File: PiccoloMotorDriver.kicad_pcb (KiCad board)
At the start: 6 copper layers, 55 x 50 mm, 128 parts, among them J1 01x03_MotorTerminal, J10 AUX2, J11 C189893, J12 C265111, J3 C189893, J4 C225127, J5 Screw_Terminal_01x02_POWER, J6 Connector, USB-TYPE-C-16P, J7 C225127, J8 AUX0, J9 AUX1, U1 SP485EEN, U2 XC6210B332MR, U3 XL1509, U4 TJA1050T/CM,118, U5 AS5047D, U6 USBLC6-2SC6, U7 STM32H723VGHx, U8 DRV8316RRGFR, X2 X322516MLB4SI

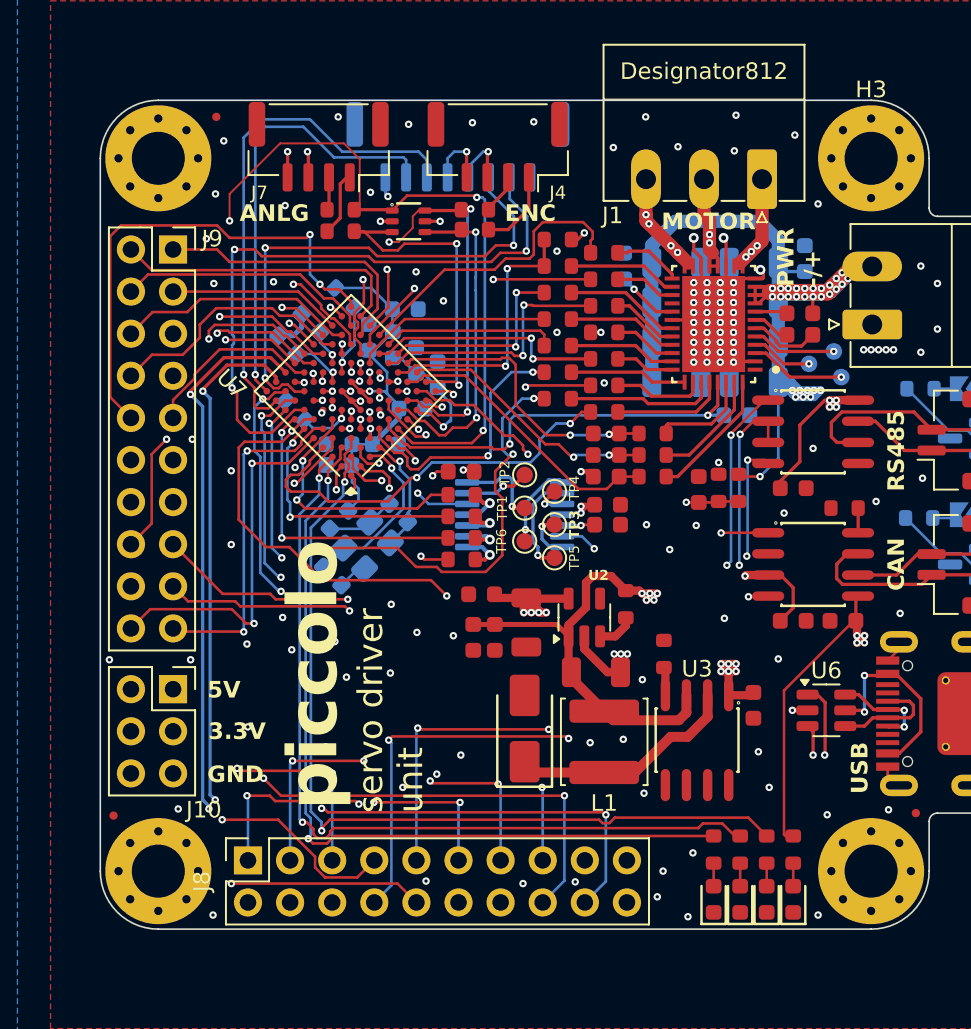
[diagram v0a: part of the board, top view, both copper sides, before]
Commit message: Started discrete inverter version
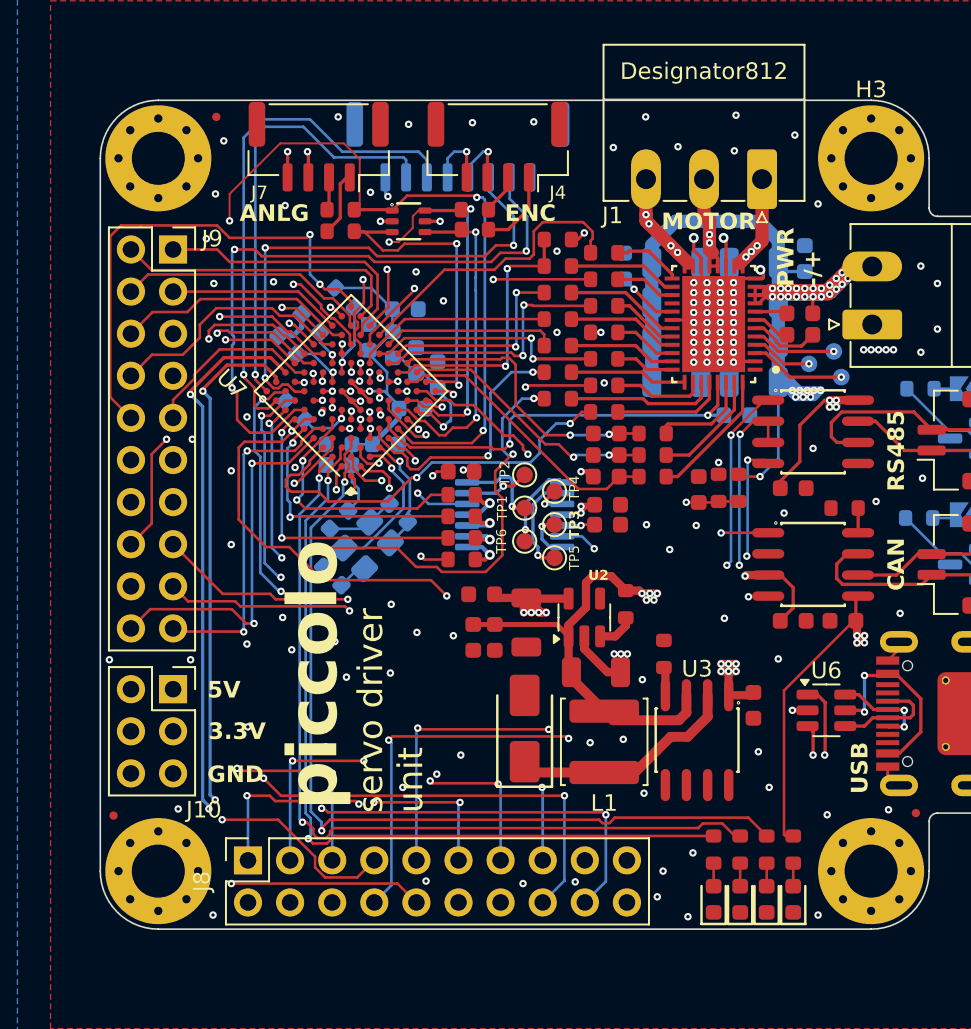
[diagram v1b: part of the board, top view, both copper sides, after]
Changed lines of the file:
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@@
 			(size 0.6 0.6)
 			(drill 0.6)
-			(layers "F&B.Cu" "*.Mask")
+			(layers "*.Cu" "*.Mask")
 		)
 		(pad "" np_thru_hole circle
@@
 			(size 0.6 0.6)
 			(drill 0.6)
-			(layers "F&B.Cu" "*.Mask")
+			(layers "*.Cu" "*.Mask")
 		)
 		(pad "A5" smd rect
@@
 		(tags "connector JST GH horizontal")
 		(property "Reference" "J12"
-			(at 0 3.9 0)
+			(at -3.425 3.9 0)
 			(layer "B.SilkS")
 			(effects
@@
 	)
 	(gr_line
-		(start 167.5 82)
-		(end 163.5 82)
+		(start 113.000026 78.500026)
+		(end 113 121.5)
 		(stroke
 			(width 0.1)
-			(type solid)
+			(type default)
 		)
 		(layer "Edge.Cuts")
 	)
 	(gr_arc
-		(start 163.5 82)
-		(mid 163.146447 81.853553)
-		(end 163 81.5)
+		(start 113.000026 78.500026)
+		(mid 114.025152 76.025152)
+		(end 116.500026 75.000026)
 		(stroke
 			(width 0.1)
@@
 		(layer "Edge.Cuts")
 	)
-	(gr_arc
-		(start 167.5 82)
-		(mid 167.853553 82.146447)
-		(end 168 82.5)
+	(gr_line
+		(start 116.5 125.000026)
+		(end 159.499974 125)
 		(stroke
 			(width 0.1)
@@
 	(gr_line
 		(start 159.500026 75.000026)
-		(end 116.500026 75.000026)
+		(end 116.5 75)
 		(stroke
 			(width 0.1)
@@
 		(layer "Edge.Cuts")
 	)
-	(gr_line
-		(start 163.000004 81.5)
-		(end 163.000026 78.507513)
+	(gr_arc
+		(start 159.500026 75.000026)
+		(mid 161.9749 76.025152)
+		(end 163.000026 78.500026)
 		(stroke
 			(width 0.1)
@@
 	)
 	(gr_line
+		(start 163.000004 81.5)
+		(end 163.000026 78.507513)
+		(stroke
+			(width 0.1)
+			(type default)
+		)
+		(layer "Edge.Cuts")
+	)
+	(gr_arc
+		(start 163.000026 121.500026)
+		(mid 161.9749 123.9749)
+		(end 159.500026 125.000026)
+		(stroke
+			(width 0.1)
+			(type default)
+		)
+		(layer "Edge.Cuts")
+	)
+	(gr_line
 		(start 163.000026 121.500026)
 		(end 163.000026 118.5)
@@
 	)
 	(gr_arc
-		(start 159.500026 75.000026)
-		(mid 161.9749 76.025152)
-		(end 163.000026 78.500026)
+		(start 163.5 82)
+		(mid 163.146447 81.853553)
+		(end 163 81.5)
 		(stroke
 			(width 0.1)
@@
 	)
 	(gr_line
-		(start 168 117.5)
-		(end 168 82.5)
+		(start 163.5 118)
+		(end 167.5 118)
 		(stroke
 			(width 0.1)
@@
 	)
 	(gr_line
-		(start 113.000026 78.500026)
-		(end 113.000026 121.500026)
+		(start 167.5 82)
+		(end 163.5 82)
 		(stroke
 			(width 0.1)
-			(type default)
+			(type solid)
 		)
 		(layer "Edge.Cuts")
 	)
 	(gr_arc
-		(start 113.000026 78.500026)
-		(mid 114.025152 76.025152)
-		(end 116.500026 75.000026)
+		(start 167.5 82)
+		(mid 167.853553 82.146447)
+		(end 168 82.5)
 		(stroke
 			(width 0.1)
@@
 	)
 	(gr_line
-		(start 116.500026 125.000026)
-		(end 159.500026 125.000026)
-		(stroke
-			(width 0.1)
-			(type default)
-		)
-		(layer "Edge.Cuts")
-	)
-	(gr_line
-		(start 163.5 118)
-		(end 167.5 118)
+		(start 168 117.5)
+		(end 168 82.5)
 		(stroke
 			(width 0.1)
@@
 		(layer "Edge.Cuts")
 	)
-	(gr_arc
-		(start 163.000026 121.500026)
-		(mid 161.9749 123.9749)
-		(end 159.500026 125.000026)
-		(stroke
-			(width 0.1)
-			(type default)
+	(gr_text "5V"
+		(at 119.45 111.15 0)
+		(layer "F.SilkS" knockout)
+		(effects
+			(font
+				(size 1 1)
+				(thickness 0.25)
+				(bold yes)
+			)
+			(justify left bottom)
 		)
-		(layer "Edge.Cuts")
 	)
 	(gr_text "GND"
@@
 		)
 	)
-	(gr_text "MOTOR"
-		(at 146.85 82.9 0)
+	(gr_text "3.3V"
+		(at 119.5 113.65 0)
 		(layer "F.SilkS" knockout)
 		(effects
@@
 		)
 	)
+	(gr_text "ENC"
+		(at 137.4 82.4 0)
+		(layer "F.SilkS" knockout)
+		(effects
+			(font
+				(size 1 1)
+				(thickness 0.25)
+				(bold yes)
+			)
+			(justify left bottom)
+		)
+	)
+	(gr_text "MOTOR"
+		(at 146.85 82.9 0)
+		(layer "F.SilkS" knockout)
+		(effects
+			(font
+				(size 1 1)
+				(thickness 0.25)
+				(bold yes)
+			)
+			(justify left bottom)
+		)
+	)
+	(gr_text "PWR\n-/+"
+		(at 156.55 86.25 90)
+		(layer "F.SilkS" knockout)
+		(effects
+			(font
+				(size 1 1)
+				(thickness 0.25)
+				(bold yes)
+			)
+			(justify left bottom)
+		)
+	)
 	(gr_text "USB"
 		(at 159.4 116.85 90)
@@
 		)
 	)
+	(gr_text "RS485"
+		(at 161.6 98.6 90)
+		(layer "F.SilkS" knockout)
+		(effects
+			(font
+				(size 1 1)
+				(thickness 0.25)
+				(bold yes)
+			)
+			(justify left bottom)
+		)
+	)
+	(gr_text "CAN"
+		(at 161.6 104.6 90)
+		(layer "F.SilkS" knockout)
+		(effects
+			(font
+				(size 1 1)
+				(thickness 0.25)
+				(bold yes)
+			)
+			(justify left bottom)
+		)
+	)
 	(gr_text "servo driver \nunit"
 		(at 132.6 118 90)
@@
 		)
 	)
-	(gr_text "CAN"
-		(at 161.6 104.6 90)
-		(layer "F.SilkS" knockout)
-		(effects
-			(font
-				(size 1 1)
-				(thickness 0.25)
-				(bold yes)
-			)
-			(justify left bottom)
-		)
-	)
-	(gr_text "RS485"
-		(at 161.6 98.6 90)
-		(layer "F.SilkS" knockout)
-		(effects
-			(font
-				(size 1 1)
-				(thickness 0.25)
-				(bold yes)
-			)
-			(justify left bottom)
-		)
-	)
-	(gr_text "PWR\n-/+"
-		(at 156.55 86.25 90)
-		(layer "F.SilkS" knockout)
-		(effects
-			(font
-				(size 1 1)
-				(thickness 0.25)
-				(bold yes)
-			)
-			(justify left bottom)
-		)
-	)
 	(gr_text "piccolo"
 		(at 127.6 117.8 90)
@@
 		)
 	)
-	(gr_text "ENC"
-		(at 137.4 82.4 0)
-		(layer "F.SilkS" knockout)
-		(effects
-			(font
-				(size 1 1)
-				(thickness 0.25)
-				(bold yes)
-			)
-			(justify left bottom)
-		)
-	)
-	(gr_text "3.3V"
-		(at 119.5 113.65 0)
-		(layer "F.SilkS" knockout)
-		(effects
-			(font
-				(size 1 1)
-				(thickness 0.25)
-				(bold yes)
-			)
-			(justify left bottom)
-		)
-	)
-	(gr_text "5V"
-		(at 119.45 111.15 0)
-		(layer "F.SilkS" knockout)
-		(effects
-			(font
-				(size 1 1)
-				(thickness 0.25)
-				(bold yes)
-			)
-			(justify left bottom)
-		)
-	)
-	(gr_text "CAN \nTermination"
-		(at 157.6 103 0)
+	(gr_text "DEBUG"
+		(at 137.8 82.25 0)
 		(layer "B.SilkS" knockout)
 		(effects
@@
 		)
 	)
-	(gr_text "DEBUG"
-		(at 137.8 82.25 0)
+	(gr_text "RS485\nTermination"
+		(at 157.6 99.2 0)
 		(layer "B.SilkS" knockout)
 		(effects
@@
 		)
 	)
-	(gr_text "RS485\nTermination"
-		(at 157.6 99.2 0)
+	(gr_text "CAN \nTermination"
+		(at 157.6 103 0)
 		(layer "B.SilkS" knockout)
 		(effects

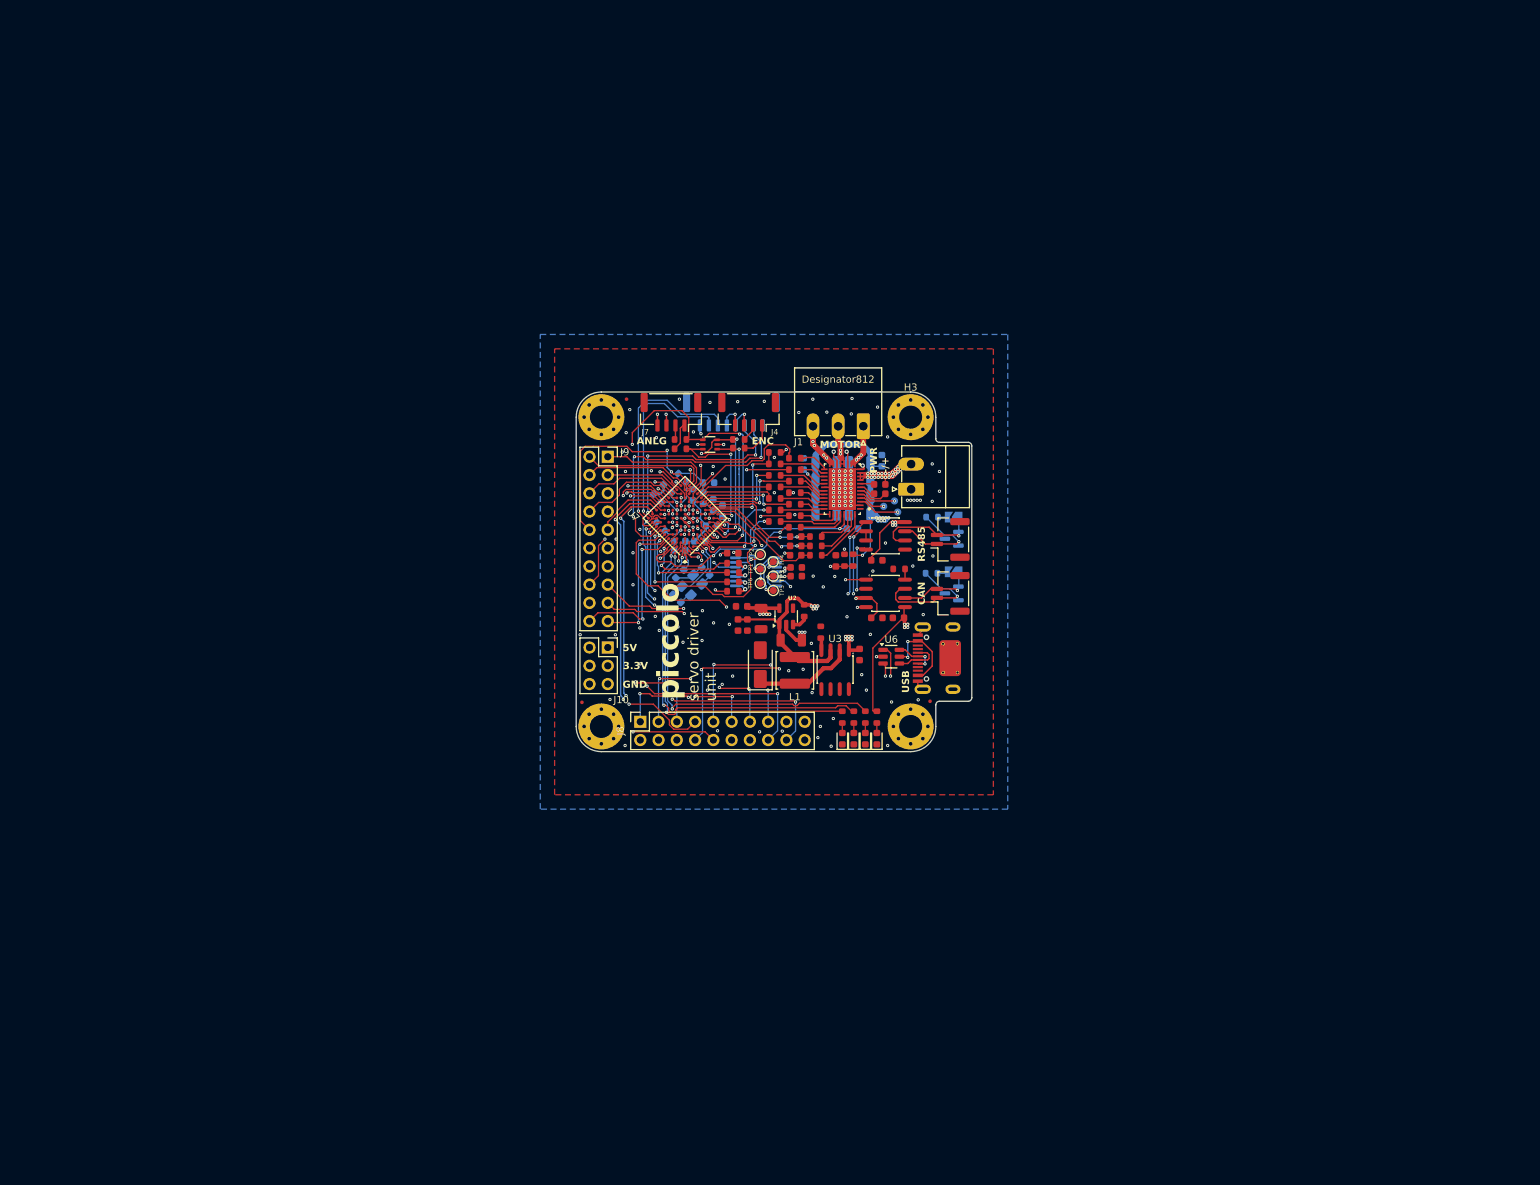
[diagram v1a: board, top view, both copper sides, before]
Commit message: added drv8353, stm32h723vgt6
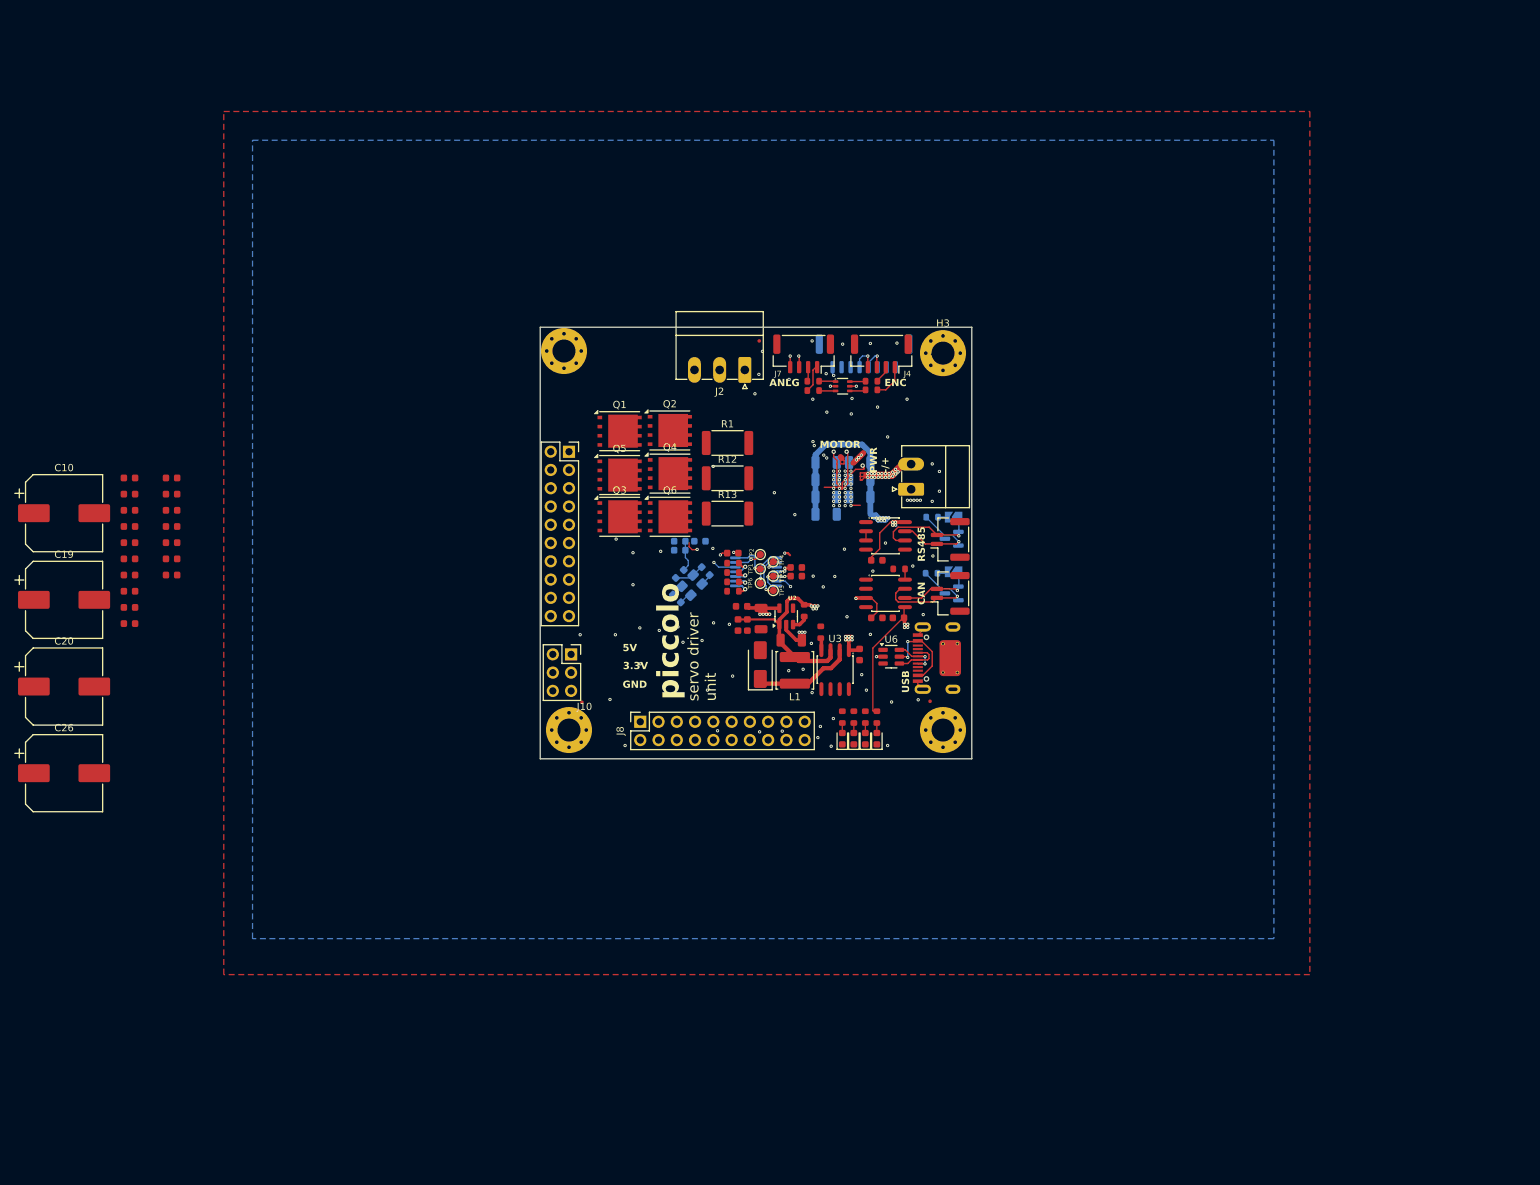
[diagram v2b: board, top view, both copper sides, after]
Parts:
- removed C39: 100nF, PCM_JLCPCB:C_0603
- removed FB2: ~, PCM_JLCPCB:FB_0603
- removed J1: 01x03_MotorTerminal, Connector_Phoenix_MC:PhoenixContact_MC_1,5_3-G-3.5_1x03_P3.50mm_Horizontal
- removed R10, R11, R14, R15, R16, R17, R18, R19, R2, R20, R26, R9: 22Ω, PCM_JLCPCB:R_0603
- removed R23, R31, R5, R7: 1kΩ, PCM_JLCPCB:R_0603
- removed R25: 10kΩ, PCM_JLCPCB:R_0603
- removed R32: 47kΩ, PCM_JLCPCB:R_0603
- removed TP7: GND_BK, TestPoint:TestPoint_Pad_D1.0mm
- removed TP8: FB_BK, TestPoint:TestPoint_Pad_D1.0mm
- removed TP9: SW_BK, TestPoint:TestPoint_Pad_D1.0mm
- removed U7: STM32H723VGHx, Package_BGA:TFBGA-100_8x8mm_Layout10x10_P0.8mm
- removed U8: DRV8316RRGFR, DRV8316:RGF0040E-IPC_A
- added C10: 100uF / 100V, Capacitor_SMD:CP_Elec_10x10.5, F.Cu at (41.8, 91.8)
- added C19: 100uF / 100V, Capacitor_SMD:CP_Elec_10x10.5, F.Cu at (41.8, 103.9)
- added C20: 100uF / 100V, Capacitor_SMD:CP_Elec_10x10.5, F.Cu at (41.8, 116.0)
- added C26: 100uF / 100V, Capacitor_SMD:CP_Elec_10x10.5, F.Cu at (41.8, 128.0)
- added C54: 1uF, PCM_JLCPCB:C_0603, F.Cu at (50.9, 107.2)
- added J2: 01x03_MotorTerminal, Connector_Phoenix_MC:PhoenixContact_MC_1,5_3-G-3.5_1x03_P3.50mm_Horizontal, F.Cu at (136.4, 71.9)
- added Q1: NE006NG, Package_DFN_QFN:AO_DFN-8-1EP_5.55x5.2mm_P1.27mm_EP4.12x4.6mm, F.Cu at (119.0, 80.5)
- added Q2: NE006NG, Package_DFN_QFN:AO_DFN-8-1EP_5.55x5.2mm_P1.27mm_EP4.12x4.6mm, F.Cu at (126.0, 80.3)
- added Q3: NE006NG, Package_DFN_QFN:AO_DFN-8-1EP_5.55x5.2mm_P1.27mm_EP4.12x4.6mm, F.Cu at (119.0, 92.3)
- added Q4: NE006NG, Package_DFN_QFN:AO_DFN-8-1EP_5.55x5.2mm_P1.27mm_EP4.12x4.6mm, F.Cu at (126.0, 86.3)
- added Q5: NE006NG, Package_DFN_QFN:AO_DFN-8-1EP_5.55x5.2mm_P1.27mm_EP4.12x4.6mm, F.Cu at (119.0, 86.5)
- added Q6: NE006NG, Package_DFN_QFN:AO_DFN-8-1EP_5.55x5.2mm_P1.27mm_EP4.12x4.6mm, F.Cu at (126.0, 92.3)
- C1, C2, C28, C29, C34, C35, C36: moved to F.Cu
- C11, C12: value 100nF -> 1nF; moved to F.Cu
- C16: value 1uF -> 100nF
- C17: value 100nF -> 47nF; moved to F.Cu
- C27: value 1nF -> 100nF
- C37: value 47nF -> 1uF
- C38: value 10uF -> 100nF; footprint PCM_JLCPCB:C_1206 -> PCM_JLCPCB:C_0603; moved to F.Cu
- C5: value 1nF -> 1uF
- R1: value 10kΩ -> 5mR; footprint PCM_JLCPCB:R_0603 -> Resistor_SMD:R_2512_6332Metric
- R12, R13: value 22Ω -> 5mR; footprint PCM_JLCPCB:R_0603 -> Resistor_SMD:R_2512_6332Metric
- moved C17 105.5 mm to (50.9, 98.2), turned to 0 degrees
- moved C37 105.2 mm to (50.9, 102.7)
- moved C16 104.6 mm to (50.9, 96.0)
- moved C38 102.3 mm to (50.9, 105.0), turned to 0 degrees
- moved C11 100.5 mm to (50.9, 91.5)
- moved C12 94.1 mm to (50.9, 93.7), turned to 0 degrees
- moved C5 93.1 mm to (50.9, 87.0), turned to 0 degrees
- moved C6 92.8 mm to (50.9, 89.2), turned to 0 degrees
- moved C27 92.7 mm to (50.9, 100.5), turned to 0 degrees
- moved C29 76.6 mm to (56.7, 93.7), turned to 0 degrees
- moved C35 75.4 mm to (56.7, 98.2)
- moved C36 75.4 mm to (56.7, 100.5)
- moved C28 75.3 mm to (56.7, 91.5), turned to 0 degrees
- moved C34 72.8 mm to (56.7, 96.0), turned to 0 degrees
- moved C1 69.0 mm to (56.7, 87.0), turned to 0 degrees
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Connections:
- C11 pad 1: DRV_AN_REF -> AN_DRV_SO_C
- C12 pad 1: +3.3V -> AN_DRV_SO_B
- C16 pad 1: Net-(U8-CP) -> AN_VBUS
- C16 pad 2: Vdrive -> GND
- C17 pad 1: Vdrive -> Net-(U7-CPL)
- C17 pad 2: GND -> Net-(U7-CPH)
- C27 pad 1: AN_DRV_SO_A -> +3.3V
- C37 pad 1: Net-(U8-CPH) -> GND
- C5 pad 1: AN_DRV_SO_B -> Net-(U7-VCP)
- C5 pad 2: GND -> Vdrive
- C6 pad 1: AN_DRV_SO_C -> AN_DRV_SO_A
- R1 pad 1: ~{DRV_FAULT} -> Net-(Q6-S)
- R1 pad 2: +3.3V -> GND
- R12 pad 1: PWM_C_H -> Net-(Q4-S)
- R12 pad 2: Net-(U8-INHC) -> GND
- R13 pad 1: PWM_C_L -> Net-(Q2-S)
- R13 pad 2: Net-(U8-INLC) -> GND
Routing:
- net USB-: track 77.4 -> 0.00 mm, vias 3 -> 0
- net USB+: track 71.9 -> 0.00 mm, vias 3 -> 0
- net /Mcu/PC9: track 67.2 -> 0.00 mm, vias 1 -> 0
- net /Mcu/PE15: track 60.2 -> 0.00 mm, vias 3 -> 0
- net /Mcu/PC6: track 53.8 -> 0.00 mm, vias 3 -> 0
- net UI_LED_YELLOW: track 53.0 -> 0.00 mm, vias 2 -> 0
- net RS485_DI: track 51.9 -> 0.00 mm, vias 4 -> 0
- net RS485_RO: track 51.1 -> 0.00 mm, vias 4 -> 0
- net UI_LED_BLUE: track 50.7 -> 0.00 mm, vias 2 -> 0
- net /Mcu/PA10: track 49.9 -> 0.00 mm, vias 2 -> 0
- net /Mcu/PD6: track 49.6 -> 0.00 mm, vias 3 -> 0
- net UI_LED_RED: track 49.4 -> 0.00 mm, vias 2 -> 0
- net /Mcu/PB15: track 49.1 -> 0.00 mm, vias 1 -> 0
- net /Mcu/PD7: track 48.6 -> 0.00 mm, vias 3 -> 0
- net RS485_DE: track 49.6 -> 1.28 mm, vias 4 -> 0
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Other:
- board size 55 x 50 mm -> 60 x 60 mm
